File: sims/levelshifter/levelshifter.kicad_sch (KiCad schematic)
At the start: 8 parts, among them Q1 BSS138

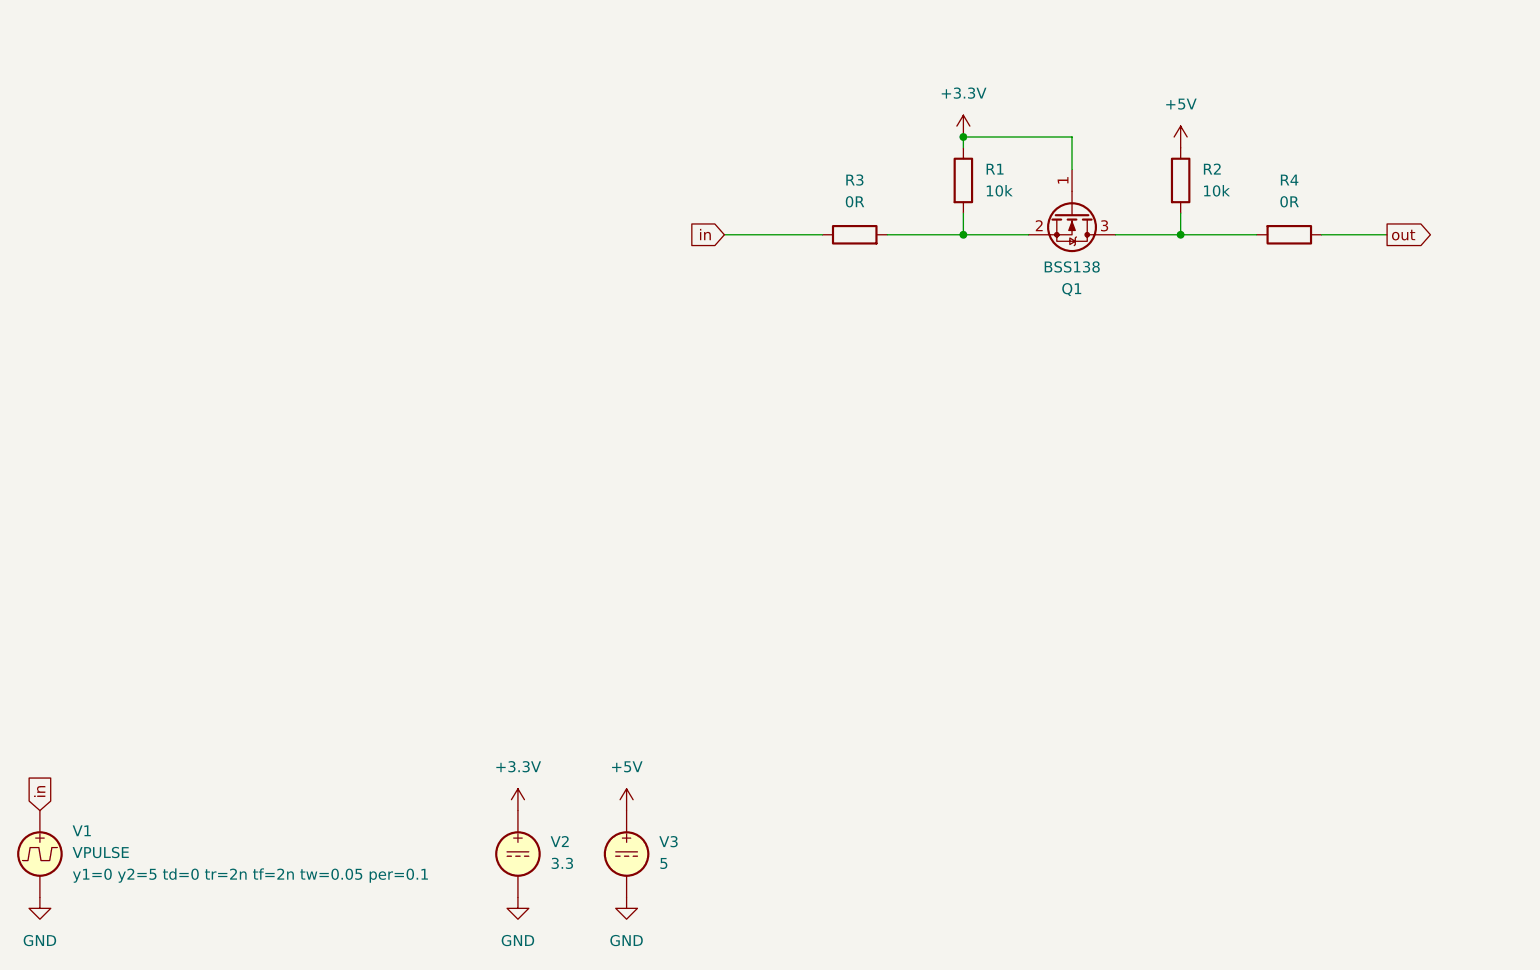
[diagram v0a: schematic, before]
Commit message: add debug led, make bulk caps smaller, export plate and bottom for rudimentary case
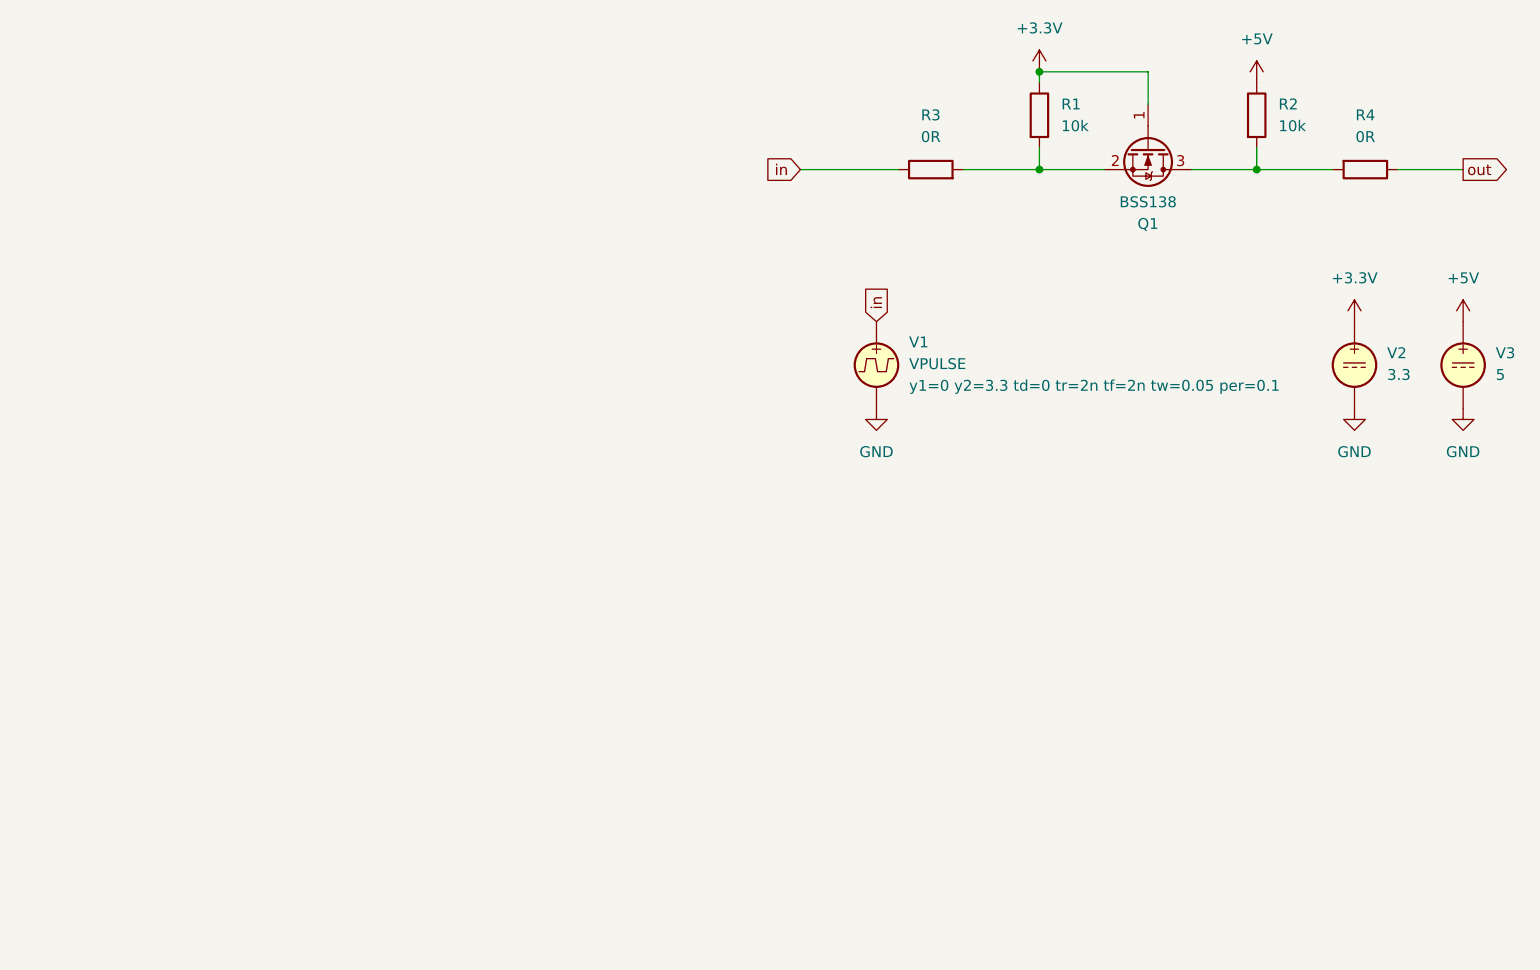
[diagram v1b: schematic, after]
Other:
- moved on the sheet: Q1, R1, R2, R3, R4, V1, V2, V3
